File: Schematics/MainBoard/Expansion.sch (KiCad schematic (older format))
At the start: 6 parts, among them J17 Device 2, J18 Device 5, J19 Device 3, J20 Device 6, J21 Device 4, J22 Device 7

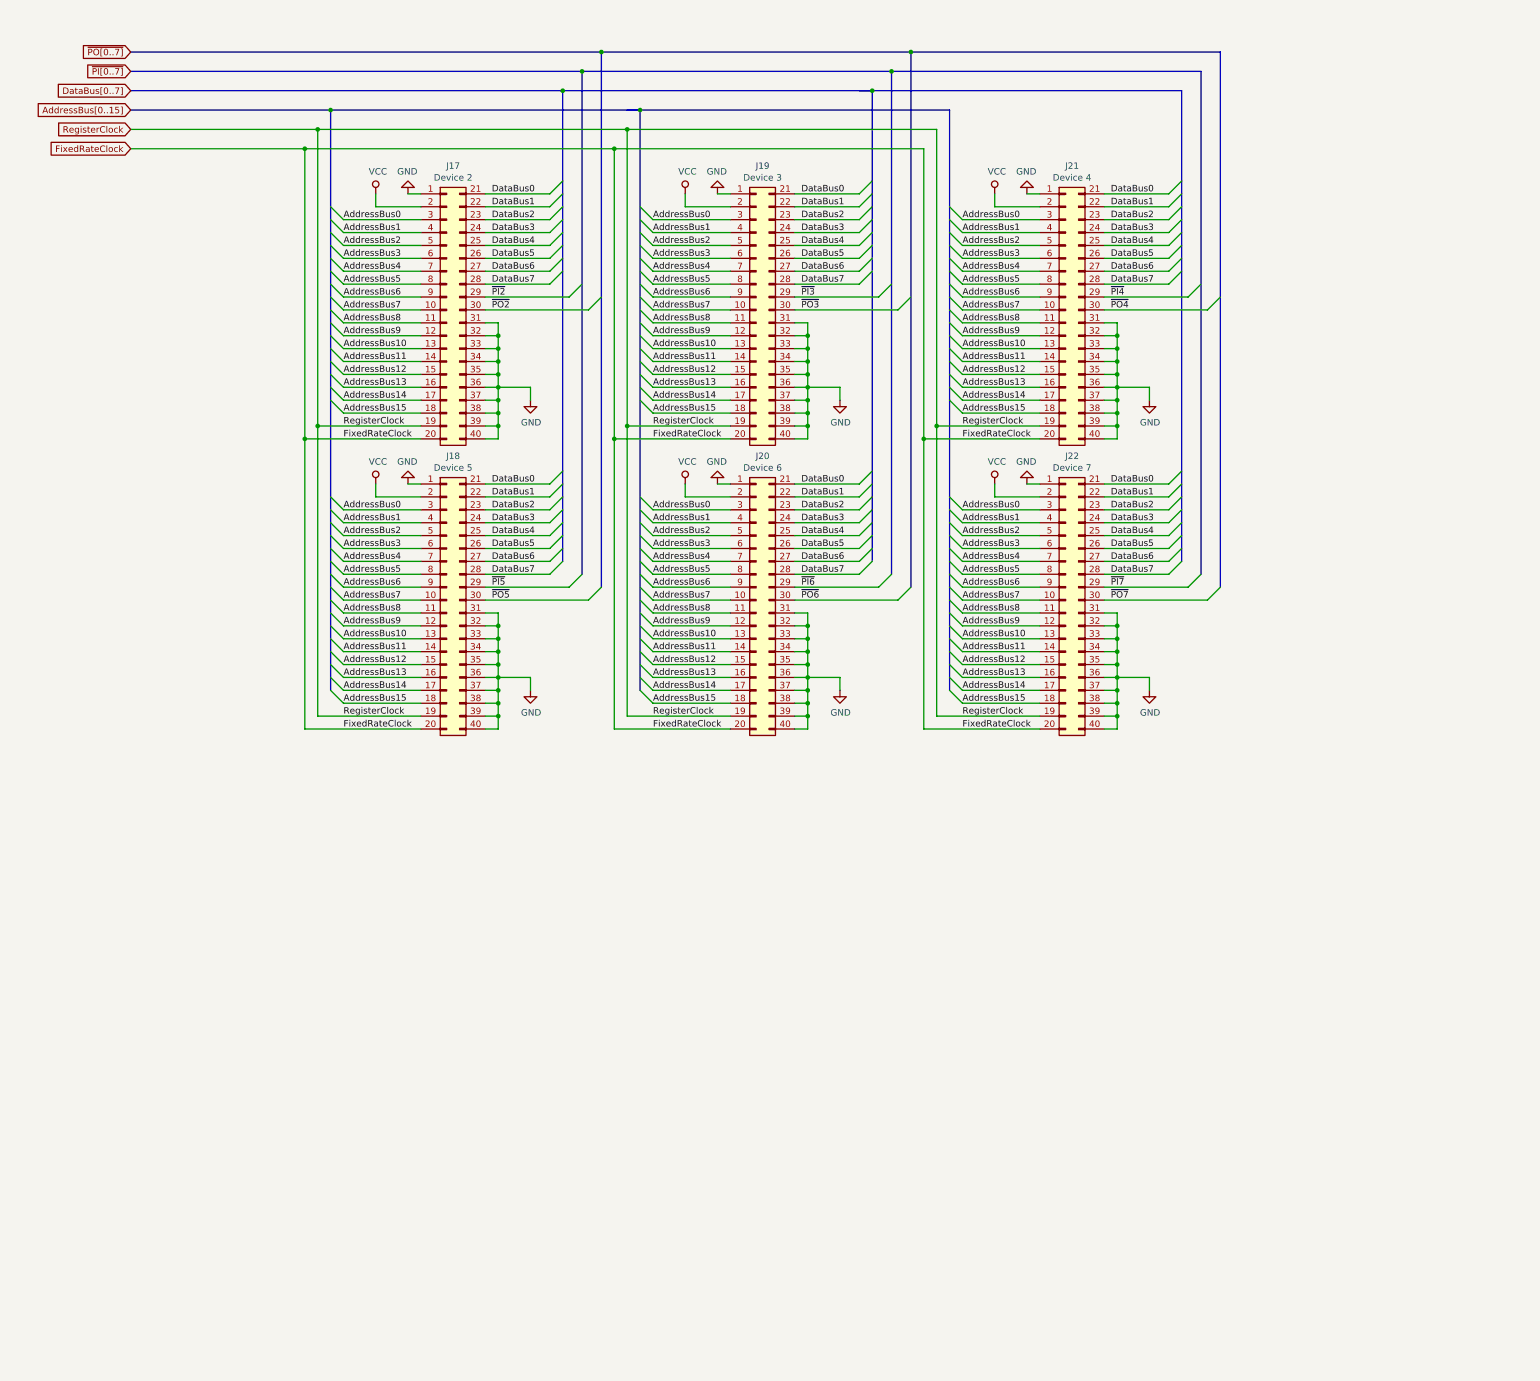
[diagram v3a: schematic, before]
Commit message: Begin work on the Rev 2 hardware.
* Four layer PCB for the main board
* Breaking the main board up into several smaller daughter boaeds.
* ZIF sockets for Instruction ROM
* Dual Port SRAM for Instruction RAM
* Daughter board connectors interleave signals and GND.
* DC Barrel jack connector for power
* WIP shifter circuit
* Rename SharedMemoryArduinoSerialCard to SerialCard.
* TurtleTTL Rev 2 will use the shared memory serial card.
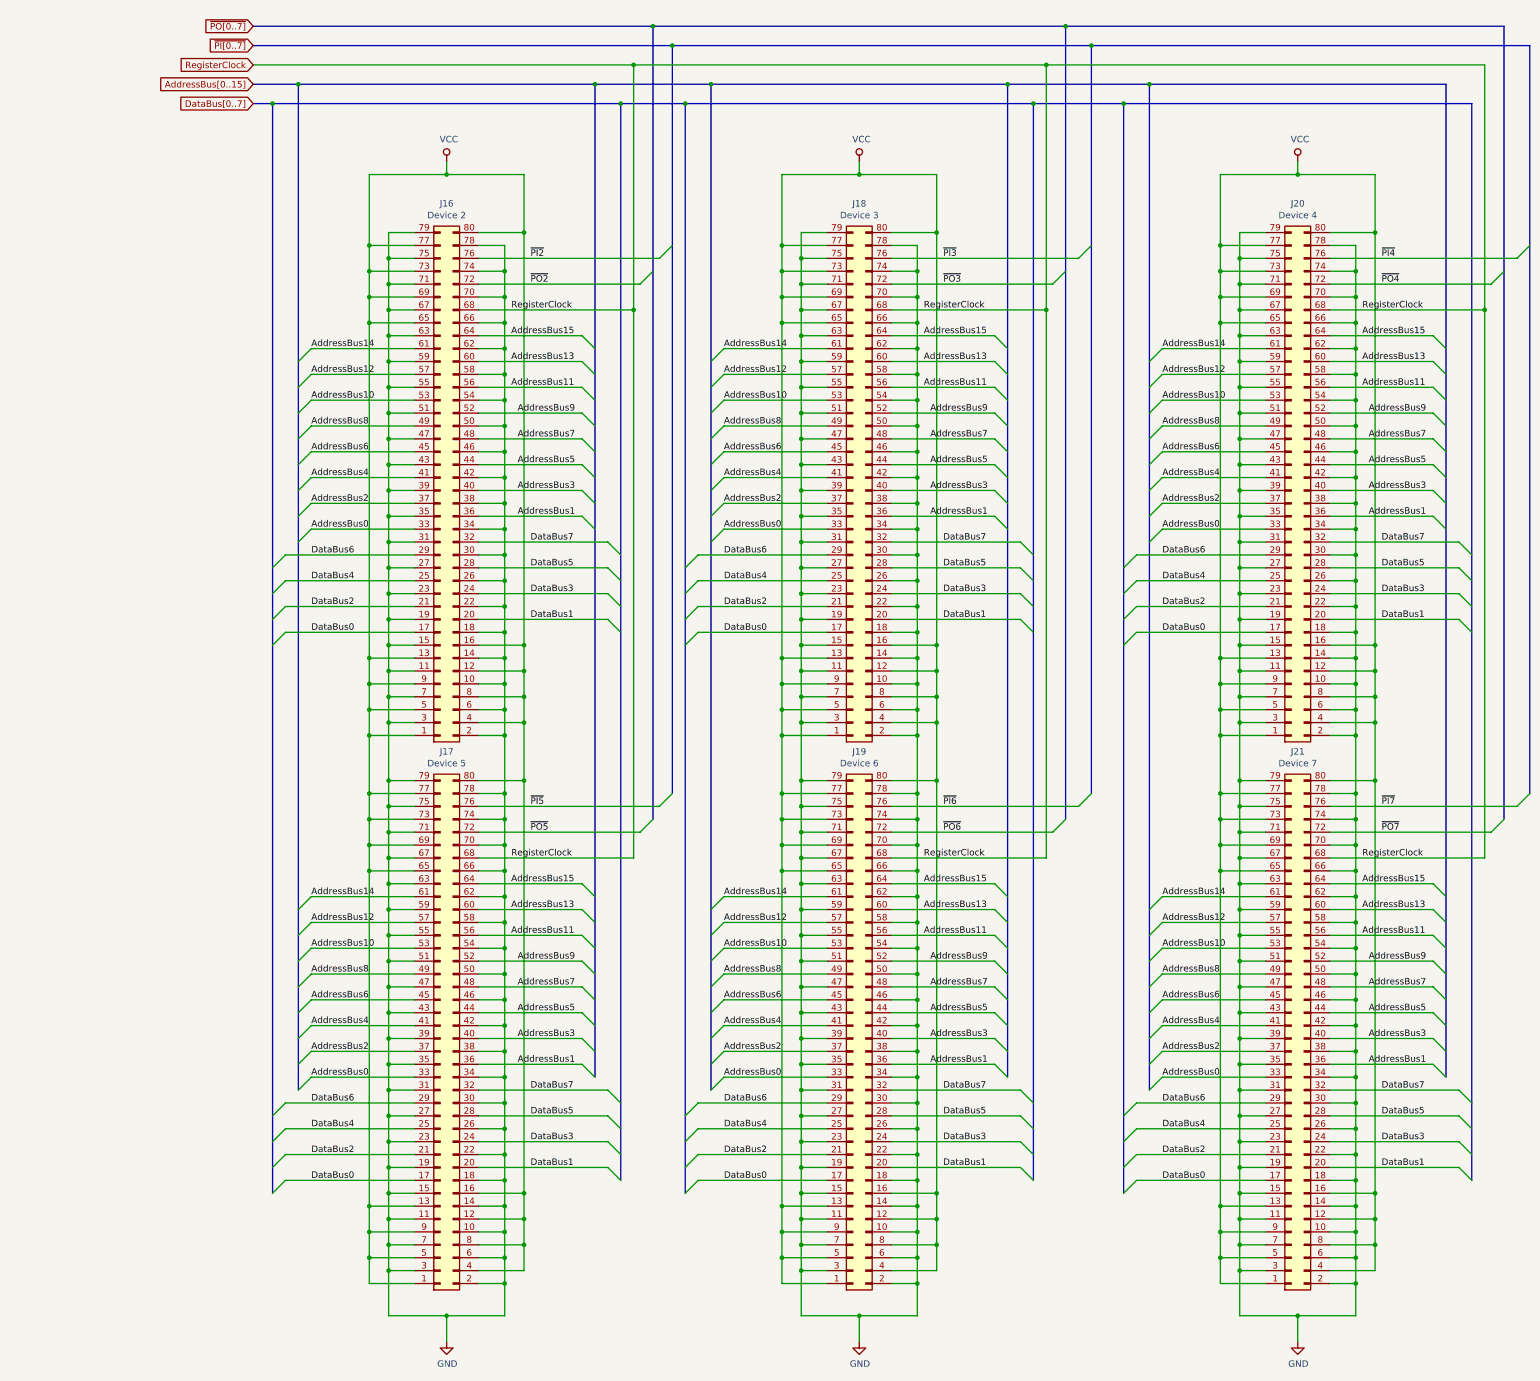
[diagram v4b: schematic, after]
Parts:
- removed J17: Device 2, Connector_PinSocket_2.54mm:PinSocket_2x20_P2.54mm_Vertical, symbol Connector_Generic:Conn_02x20_Top_Bottom
- removed J18: Device 5, Connector_PinSocket_2.54mm:PinSocket_2x20_P2.54mm_Vertical, symbol Connector_Generic:Conn_02x20_Top_Bottom
- removed J19: Device 3, Connector_PinSocket_2.54mm:PinSocket_2x20_P2.54mm_Vertical, symbol Connector_Generic:Conn_02x20_Top_Bottom
- removed J20: Device 6, Connector_PinSocket_2.54mm:PinSocket_2x20_P2.54mm_Vertical, symbol Connector_Generic:Conn_02x20_Top_Bottom
- removed J21: Device 4, Connector_PinSocket_2.54mm:PinSocket_2x20_P2.54mm_Vertical, symbol Connector_Generic:Conn_02x20_Top_Bottom
- removed J22: Device 7, Connector_PinSocket_2.54mm:PinSocket_2x20_P2.54mm_Vertical, symbol Connector_Generic:Conn_02x20_Top_Bottom
- added J16: Device 2, Connector_PinSocket_2.54mm:PinSocket_2x40_P2.54mm_Vertical, symbol Connector_Generic:Conn_02x40_Odd_Even
- added J17: Device 5, Connector_PinSocket_2.54mm:PinSocket_2x40_P2.54mm_Vertical, symbol Connector_Generic:Conn_02x40_Odd_Even
- added J18: Device 3, Connector_PinSocket_2.54mm:PinSocket_2x40_P2.54mm_Vertical, symbol Connector_Generic:Conn_02x40_Odd_Even
- added J19: Device 6, Connector_PinSocket_2.54mm:PinSocket_2x40_P2.54mm_Vertical, symbol Connector_Generic:Conn_02x40_Odd_Even
- added J20: Device 4, Connector_PinSocket_2.54mm:PinSocket_2x40_P2.54mm_Vertical, symbol Connector_Generic:Conn_02x40_Odd_Even
- added J21: Device 7, Connector_PinSocket_2.54mm:PinSocket_2x40_P2.54mm_Vertical, symbol Connector_Generic:Conn_02x40_Odd_Even
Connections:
- net AddressBus0: now also J16.33 (Pin_33), J17.33 (Pin_33), J18.33 (Pin_33), J19.33 (Pin_33), J20.33 (Pin_33), J21.33 (Pin_33)
- net AddressBus1: now also J16.36 (Pin_36), J17.36 (Pin_36), J18.36 (Pin_36), J19.36 (Pin_36), J20.36 (Pin_36), J21.36 (Pin_36)
- net AddressBus10: now also J16.53 (Pin_53), J17.53 (Pin_53), J18.53 (Pin_53), J19.53 (Pin_53), J20.53 (Pin_53), J21.53 (Pin_53)
- net AddressBus11: now also J16.56 (Pin_56), J17.56 (Pin_56), J18.56 (Pin_56), J19.56 (Pin_56), J20.56 (Pin_56), J21.56 (Pin_56)
- net AddressBus12: now also J16.57 (Pin_57), J17.57 (Pin_57), J18.57 (Pin_57), J19.57 (Pin_57), J20.57 (Pin_57), J21.57 (Pin_57)
- net AddressBus13: now also J16.60 (Pin_60), J17.60 (Pin_60), J18.60 (Pin_60), J19.60 (Pin_60), J20.60 (Pin_60), J21.60 (Pin_60)
- net AddressBus14: now also J16.61 (Pin_61), J17.61 (Pin_61), J18.61 (Pin_61), J19.61 (Pin_61), J20.61 (Pin_61), J21.61 (Pin_61)
- net AddressBus15: now also J16.64 (Pin_64), J17.64 (Pin_64), J18.64 (Pin_64), J19.64 (Pin_64), J20.64 (Pin_64), J21.64 (Pin_64)
- net AddressBus2: now also J16.37 (Pin_37), J17.37 (Pin_37), J18.37 (Pin_37), J19.37 (Pin_37), J20.37 (Pin_37), J21.37 (Pin_37)
- net AddressBus3: now also J16.40 (Pin_40), J17.40 (Pin_40), J18.40 (Pin_40), J19.40 (Pin_40), J20.40 (Pin_40), J21.40 (Pin_40)
- net AddressBus4: now also J16.41 (Pin_41), J17.41 (Pin_41), J18.41 (Pin_41), J19.41 (Pin_41), J20.41 (Pin_41), J21.41 (Pin_41)
- net AddressBus5: now also J16.44 (Pin_44), J17.44 (Pin_44), J18.44 (Pin_44), J19.44 (Pin_44), J20.44 (Pin_44), J21.44 (Pin_44)
- net AddressBus6: now also J16.45 (Pin_45), J17.45 (Pin_45), J18.45 (Pin_45), J19.45 (Pin_45), J20.45 (Pin_45), J21.45 (Pin_45)
- net AddressBus7: now also J16.48 (Pin_48), J17.48 (Pin_48), J18.48 (Pin_48), J19.48 (Pin_48), J20.48 (Pin_48), J21.48 (Pin_48)
- net AddressBus8: now also J16.49 (Pin_49), J17.49 (Pin_49), J18.49 (Pin_49), J19.49 (Pin_49), J20.49 (Pin_49), J21.49 (Pin_49)
- net AddressBus9: now also J16.52 (Pin_52), J17.52 (Pin_52), J18.52 (Pin_52), J19.52 (Pin_52), J20.52 (Pin_52), J21.52 (Pin_52)
- net DataBus0: now also J16.17 (Pin_17), J17.17 (Pin_17), J18.17 (Pin_17), J19.17 (Pin_17), J20.17 (Pin_17), J21.17 (Pin_17)
- net DataBus1: now also J16.20 (Pin_20), J17.20 (Pin_20), J18.20 (Pin_20), J19.20 (Pin_20), J20.20 (Pin_20), J21.20 (Pin_20)
- net DataBus2: now also J16.21 (Pin_21), J17.21 (Pin_21), J18.21 (Pin_21), J19.21 (Pin_21), J20.21 (Pin_21), J21.21 (Pin_21)
- net DataBus3: now also J16.24 (Pin_24), J17.24 (Pin_24), J18.24 (Pin_24), J19.24 (Pin_24), J20.24 (Pin_24), J21.24 (Pin_24)
- net DataBus4: now also J16.25 (Pin_25), J17.25 (Pin_25), J18.25 (Pin_25), J19.25 (Pin_25), J20.25 (Pin_25), J21.25 (Pin_25)
- net DataBus5: now also J16.28 (Pin_28), J17.28 (Pin_28), J18.28 (Pin_28), J19.28 (Pin_28), J20.28 (Pin_28), J21.28 (Pin_28)
- net DataBus6: now also J16.29 (Pin_29), J17.29 (Pin_29), J18.29 (Pin_29), J19.29 (Pin_29), J20.29 (Pin_29), J21.29 (Pin_29)
- net DataBus7: now also J16.32 (Pin_32), J17.32 (Pin_32), J18.32 (Pin_32), J19.32 (Pin_32), J20.32 (Pin_32), J21.32 (Pin_32)
- net GND: now also J16.10 (Pin_10), J16.11 (Pin_11), J16.14 (Pin_14), J16.15 (Pin_15), J16.18 (Pin_18), J16.19 (Pin_19), J16.2 (Pin_2), J16.22 (Pin_22), J16.23 (Pin_23), J16.26 (Pin_26), J16.27 (Pin_27), J16.3 (Pin_3), J16.30 (Pin_30), J16.31 (Pin_31), J16.34 (Pin_34), J16.35 (Pin_35), J16.38 (Pin_38), J16.39 (Pin_39), J16.42 (Pin_42), J16.43 (Pin_43), J16.46 (Pin_46), J16.47 (Pin_47), J16.50 (Pin_50), J16.51 (Pin_51), J16.54 (Pin_54), J16.55 (Pin_55), J16.58 (Pin_58), J16.59 (Pin_59), J16.6 (Pin_6), J16.62 (Pin_62), J16.63 (Pin_63), J16.66 (Pin_66), J16.67 (Pin_67), J16.7 (Pin_7), J16.70 (Pin_70), J16.71 (Pin_71), J16.74 (Pin_74), J16.75 (Pin_75), J16.78 (Pin_78), J16.79 (Pin_79), J17.10 (Pin_10), J17.11 (Pin_11), J17.14 (Pin_14), J17.15 (Pin_15), J17.18 (Pin_18), J17.19 (Pin_19), J17.2 (Pin_2), J17.22 (Pin_22), J17.23 (Pin_23), J17.26 (Pin_26), J17.27 (Pin_27), J17.3 (Pin_3), J17.30 (Pin_30), J17.31 (Pin_31), J17.34 (Pin_34), J17.35 (Pin_35), J17.38 (Pin_38), J17.39 (Pin_39), J17.42 (Pin_42), J17.43 (Pin_43), J17.46 (Pin_46), J17.47 (Pin_47), J17.50 (Pin_50), J17.51 (Pin_51), J17.54 (Pin_54), J17.55 (Pin_55), J17.58 (Pin_58), J17.59 (Pin_59), J17.6 (Pin_6), J17.62 (Pin_62), J17.63 (Pin_63), J17.66 (Pin_66), J17.67 (Pin_67), J17.7 (Pin_7), J17.70 (Pin_70), J17.71 (Pin_71), J17.74 (Pin_74), J17.75 (Pin_75), J17.78 (Pin_78), J17.79 (Pin_79), J18.10 (Pin_10), J18.11 (Pin_11), J18.14 (Pin_14), J18.15 (Pin_15), J18.18 (Pin_18), J18.19 (Pin_19), J18.2 (Pin_2), J18.22 (Pin_22), J18.23 (Pin_23), J18.26 (Pin_26), J18.27 (Pin_27), J18.3 (Pin_3), J18.30 (Pin_30), J18.31 (Pin_31), J18.34 (Pin_34), J18.35 (Pin_35), J18.38 (Pin_38), J18.39 (Pin_39), J18.42 (Pin_42), J18.43 (Pin_43), J18.46 (Pin_46), J18.47 (Pin_47), J18.50 (Pin_50), J18.51 (Pin_51), J18.54 (Pin_54), J18.55 (Pin_55), J18.58 (Pin_58), J18.59 (Pin_59), J18.6 (Pin_6), J18.62 (Pin_62), J18.63 (Pin_63), J18.66 (Pin_66), J18.67 (Pin_67), J18.7 (Pin_7), J18.70 (Pin_70), J18.71 (Pin_71), J18.74 (Pin_74), J18.75 (Pin_75), J18.78 (Pin_78), J18.79 (Pin_79), J19.10 (Pin_10), J19.11 (Pin_11), J19.14 (Pin_14), J19.15 (Pin_15), J19.18 (Pin_18), J19.19 (Pin_19), J19.2 (Pin_2), J19.22 (Pin_22), J19.23 (Pin_23), J19.26 (Pin_26), J19.27 (Pin_27), J19.3 (Pin_3), J19.30 (Pin_30), J19.31 (Pin_31), J19.34 (Pin_34), J19.35 (Pin_35), J19.38 (Pin_38), J19.39 (Pin_39), J19.42 (Pin_42), J19.43 (Pin_43), J19.46 (Pin_46), J19.47 (Pin_47), J19.50 (Pin_50), J19.51 (Pin_51), J19.54 (Pin_54), J19.55 (Pin_55), J19.58 (Pin_58), J19.59 (Pin_59), J19.6 (Pin_6), J19.62 (Pin_62), J19.63 (Pin_63), J19.66 (Pin_66), J19.67 (Pin_67), J19.7 (Pin_7), J19.70 (Pin_70), J19.71 (Pin_71), J19.74 (Pin_74), J19.75 (Pin_75), J19.78 (Pin_78), J19.79 (Pin_79), J20.10 (Pin_10), J20.11 (Pin_11), J20.14 (Pin_14), J20.15 (Pin_15), J20.18 (Pin_18), J20.19 (Pin_19), J20.2 (Pin_2), J20.22 (Pin_22), J20.23 (Pin_23), J20.26 (Pin_26), J20.27 (Pin_27), J20.3 (Pin_3), J20.30 (Pin_30), J20.31 (Pin_31), J20.34 (Pin_34), J20.35 (Pin_35), J20.38 (Pin_38), J20.39 (Pin_39), J20.42 (Pin_42), J20.43 (Pin_43), J20.46 (Pin_46), J20.47 (Pin_47), J20.50 (Pin_50), J20.51 (Pin_51), J20.54 (Pin_54), J20.55 (Pin_55), J20.58 (Pin_58), J20.59 (Pin_59), J20.6 (Pin_6), J20.62 (Pin_62), J20.63 (Pin_63), J20.66 (Pin_66), J20.67 (Pin_67), J20.7 (Pin_7), J20.70 (Pin_70), J20.71 (Pin_71), J20.74 (Pin_74), J20.75 (Pin_75), J20.78 (Pin_78), J20.79 (Pin_79), J21.10 (Pin_10), J21.11 (Pin_11), J21.14 (Pin_14), J21.15 (Pin_15), J21.18 (Pin_18), J21.19 (Pin_19), J21.2 (Pin_2), J21.22 (Pin_22), J21.23 (Pin_23), J21.26 (Pin_26), J21.27 (Pin_27), J21.3 (Pin_3), J21.30 (Pin_30), J21.31 (Pin_31), J21.34 (Pin_34), J21.35 (Pin_35), J21.38 (Pin_38), J21.39 (Pin_39), J21.42 (Pin_42), J21.43 (Pin_43), J21.46 (Pin_46), J21.47 (Pin_47), J21.50 (Pin_50), J21.51 (Pin_51), J21.54 (Pin_54), J21.55 (Pin_55), J21.58 (Pin_58), J21.59 (Pin_59), J21.6 (Pin_6), J21.62 (Pin_62), J21.63 (Pin_63), J21.66 (Pin_66), J21.67 (Pin_67), J21.7 (Pin_7), J21.70 (Pin_70), J21.71 (Pin_71), J21.74 (Pin_74), J21.75 (Pin_75), J21.78 (Pin_78), J21.79 (Pin_79)
- net RegisterClock: now also J16.68 (Pin_68), J17.68 (Pin_68), J18.68 (Pin_68), J19.68 (Pin_68), J20.68 (Pin_68), J21.68 (Pin_68)
- net VCC: now also J16.1 (Pin_1), J16.12 (Pin_12), J16.13 (Pin_13), J16.16 (Pin_16), J16.4 (Pin_4), J16.5 (Pin_5), J16.65 (Pin_65), J16.69 (Pin_69), J16.73 (Pin_73), J16.77 (Pin_77), J16.8 (Pin_8), J16.80 (Pin_80), J16.9 (Pin_9), J17.1 (Pin_1), J17.12 (Pin_12), J17.13 (Pin_13), J17.16 (Pin_16), J17.4 (Pin_4), J17.5 (Pin_5), J17.65 (Pin_65), J17.69 (Pin_69), J17.73 (Pin_73), J17.77 (Pin_77), J17.8 (Pin_8), J17.80 (Pin_80), J17.9 (Pin_9), J18.1 (Pin_1), J18.12 (Pin_12), J18.13 (Pin_13), J18.16 (Pin_16), J18.4 (Pin_4), J18.5 (Pin_5), J18.65 (Pin_65), J18.69 (Pin_69), J18.73 (Pin_73), J18.77 (Pin_77), J18.8 (Pin_8), J18.80 (Pin_80), J18.9 (Pin_9), J19.1 (Pin_1), J19.12 (Pin_12), J19.13 (Pin_13), J19.16 (Pin_16), J19.4 (Pin_4), J19.5 (Pin_5), J19.65 (Pin_65), J19.69 (Pin_69), J19.73 (Pin_73), J19.77 (Pin_77), J19.8 (Pin_8), J19.80 (Pin_80), J19.9 (Pin_9), J20.1 (Pin_1), J20.12 (Pin_12), J20.13 (Pin_13), J20.16 (Pin_16), J20.4 (Pin_4), J20.5 (Pin_5), J20.65 (Pin_65), J20.69 (Pin_69), J20.73 (Pin_73), J20.77 (Pin_77), J20.8 (Pin_8), J20.80 (Pin_80), J20.9 (Pin_9), J21.1 (Pin_1), J21.12 (Pin_12), J21.13 (Pin_13), J21.16 (Pin_16), J21.4 (Pin_4), J21.5 (Pin_5), J21.65 (Pin_65), J21.69 (Pin_69), J21.73 (Pin_73), J21.77 (Pin_77), J21.8 (Pin_8), J21.80 (Pin_80), J21.9 (Pin_9)
- net ~PI2: now also J16.76 (Pin_76)
- net ~PI3: now also J18.76 (Pin_76)
- net ~PI4: now also J20.76 (Pin_76)
- net ~PI5: now also J17.76 (Pin_76)
- net ~PI6: now also J19.76 (Pin_76)
- net ~PI7: now also J21.76 (Pin_76)
- net ~PO2: now also J16.72 (Pin_72)
- net ~PO3: now also J18.72 (Pin_72)
- net ~PO4: now also J20.72 (Pin_72)
- net ~PO5: now also J17.72 (Pin_72)
- net ~PO6: now also J19.72 (Pin_72)
- net ~PO7: now also J21.72 (Pin_72)
